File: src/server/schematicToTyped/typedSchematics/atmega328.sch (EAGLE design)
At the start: 7 parts, among them U3 ATMEGA328, Y1 8MHz

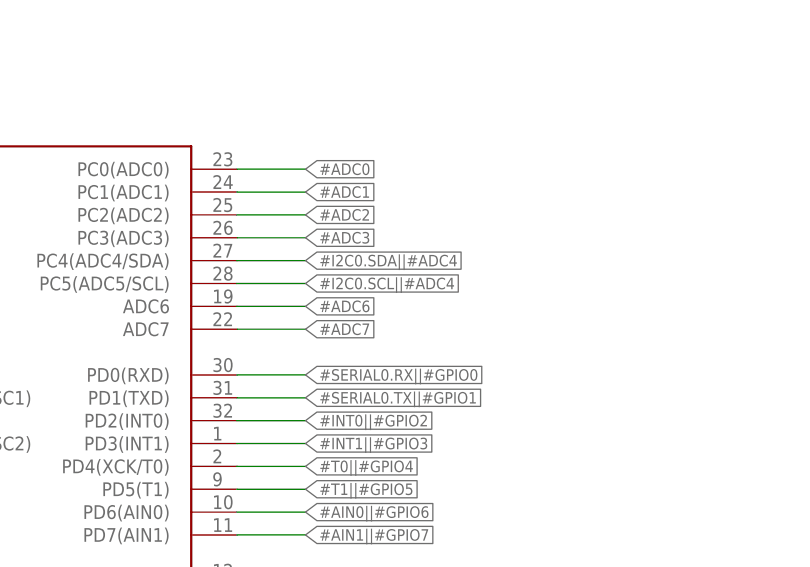
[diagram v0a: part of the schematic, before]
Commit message: Fix repeated net name
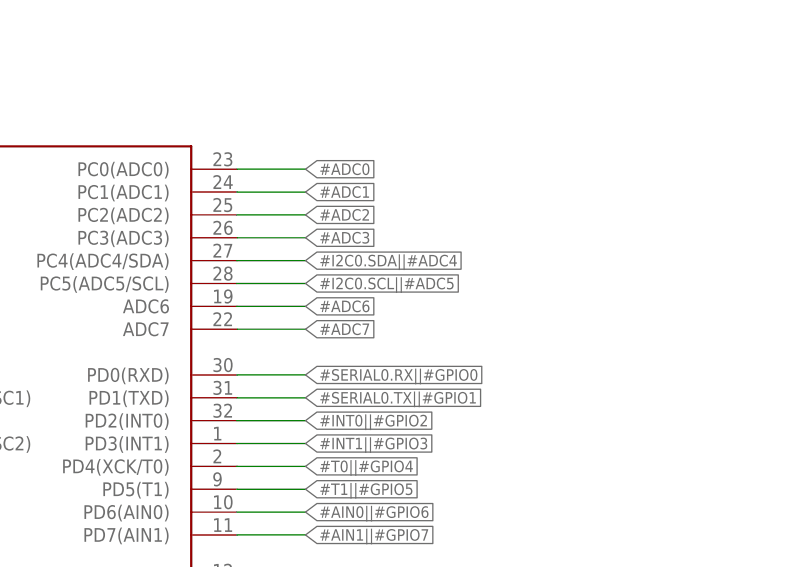
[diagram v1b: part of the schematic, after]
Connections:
- net #I2C0.SCL||#ADC4 renamed #I2C0.SCL||#ADC5
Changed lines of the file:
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@@
 </segment>
 </net>
-<net name="#I2C0.SCL||#ADC4" class="0">
+<net name="#I2C0.SCL||#ADC5" class="0">
 <segment>
 <pinref part="U3" gate="G$1" pin="PC5(ADC5/SCL)"/>

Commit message: Adding untracked schematics
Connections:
- net #ADC0 renamed !#ADC0
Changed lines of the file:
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@@
 </segment>
 </net>
-<net name="#ADC0" class="0">
+<net name="!#ADC0" class="0">
 <segment>
 <pinref part="U3" gate="G$1" pin="PC0(ADC0)"/>
